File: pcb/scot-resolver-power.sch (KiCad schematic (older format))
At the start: 36 parts, among them IC4 TSR1, U1 MCP1703A-5002_SOT223, U2 LT1762, U3 MCP1703A-5002_SOT223, U4 MCP1703A-5002_SOT223, U5 MCP1703A-3302_SOT223

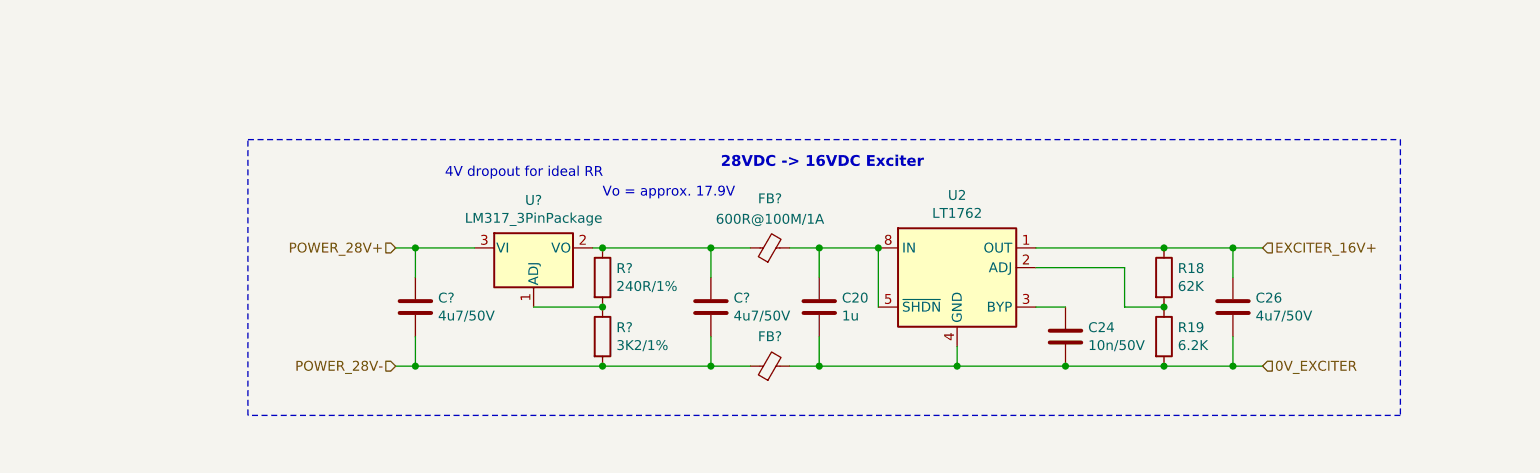
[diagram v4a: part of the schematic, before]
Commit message: pcb: V2 schematic updates (PCB still to do).
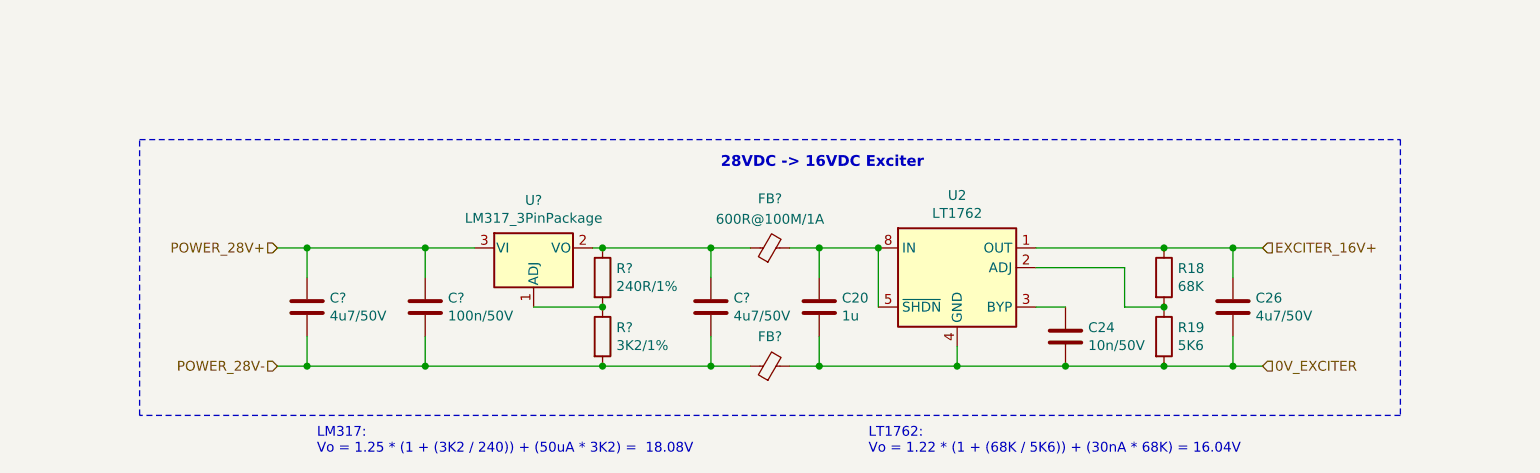
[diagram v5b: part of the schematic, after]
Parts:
- added C?: 100n/50V, Capacitor_SMD:C_0603_1608Metric_Pad1.05x0.95mm_HandSolder, symbol Device:C
- R18: value 62K -> 68K
- R19: value 6.2K -> 5K6
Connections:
- net POWER_28V+: now also C?.1
- net POWER_28V-: now also C?.2
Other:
- note added: "LM317:\nVo = 1.25 * (1 + (3K2 / 240)) + (50uA * 3K2) = 18.08V"
- note added: "LT1762:\nVo = 1.22 * (1 + (68K / 5K6)) + (30nA * 68K) = 16.04V"
- note removed: "4V dropout for ideal RR"
- note removed: "Vo = approx. 17.9V"
- moved on the sheet: C?
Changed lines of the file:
@@
 $Descr A4 11693 8268
 encoding utf-8
-Sheet 4 9
+Sheet 4 7
 Title ""
 Date ""
@@
 AR Path="/5E2C28ED/5E2DB019" Ref="R19"  Part="1"
 F 0 "R19" H 7020 5796 50  0000 L CNN
-F 1 "6.2K" H 7020 5705 50  0000 L CNN
+F 1 "5K6" H 7020 5705 50  0000 L CNN
 F 2 "Resistor_SMD:R_0603_1608Metric_Pad1.05x0.95mm_HandSolder" V 6880 5750 50  0001 C CNN
 F 3 "~" H 6950 5750 50  0001 C CNN
@@
 AR Path="/5E2C28ED/5E2DB01F" Ref="R18"  Part="1"
 F 0 "R18" H 7020 5496 50  0000 L CNN
-F 1 "62K" H 7020 5405 50  0000 L CNN
+F 1 "68K" H 7020 5405 50  0000 L CNN
 F 2 "Resistor_SMD:R_0603_1608Metric_Pad1.05x0.95mm_HandSolder" V 6880 5450 50  0001 C CNN
 F 3 "~" H 6950 5450 50  0001 C CNN
@@
 	8150 4750 8150 6150
 Wire Notes Line
-	2300 6150 2300 4750
+	1750 6150 1750 4750
 Text HLabel 2000 1700 0    50   Input ~ 0
 POWER_28V+
@@
 Connection ~ 2650 2000
 Wire Notes Line
-	2300 4750 8150 4750
-Wire Notes Line
-	8150 6150 2300 6150
+	1750 4750 8150 4750
+Wire Notes Line
+	8150 6150 1750 6150
 Wire Notes Line
 	7300 3950 10650 3950
@@
 L Device:C C?
 U 1 1 5E9EAF60
-P 3150 5600
+P 2600 5600
 AR Path="/5E9EAF60" Ref="C?"  Part="1"
 AR Path="/5E2C28ED/5E9EAF60" Ref="C?"  Part="1"
-F 0 "C?" H 3265 5646 50  0000 L CNN
-F 1 "4u7/50V" H 3265 5555 50  0000 L CNN
-F 2 "Capacitor_SMD:C_1206_3216Metric_Pad1.42x1.75mm_HandSolder" H 3188 5450 50  0001 C CNN
-F 3 "~" H 3150 5600 50  0001 C CNN
-	1    3150 5600
+F 0 "C?" H 2715 5646 50  0000 L CNN
+F 1 "4u7/50V" H 2715 5555 50  0000 L CNN
+F 2 "Capacitor_SMD:C_1206_3216Metric_Pad1.42x1.75mm_HandSolder" H 2638 5450 50  0001 C CNN
+F 3 "~" H 2600 5600 50  0001 C CNN
+	1    2600 5600
 	1    0    0    -1
 $EndComp
@@
 $EndComp
 Wire Wire Line
-	3150 5450 3150 5300
-Wire Wire Line
-	3150 5300 3450 5300
+	2600 5450 2600 5300
+Wire Wire Line
+	2600 5300 3200 5300
 Wire Wire Line
 	4050 5300 4100 5300
@@
 Connection ~ 4100 5300
 Wire Wire Line
-	4100 5900 3150 5900
-Wire Wire Line
-	3150 5900 3150 5750
+	4100 5900 3200 5900
+Wire Wire Line
+	2600 5900 2600 5750
 Connection ~ 4100 5900
-Text Notes 4100 5050 0    50   ~ 0
-Vo = approx. 17.9V
+Text Notes 2650 6350 0    50   ~ 0
+LM317:\nVo = 1.25 * (1 + (3K2 / 240)) + (50uA * 3K2) =  18.08V
 Text HLabel 7450 5900 2    50   Input ~ 0
 0V_EXCITER
@@
 	7450 5900 7300 5900
 Connection ~ 7300 5900
-Text Notes 3300 4950 0    50   ~ 0
-4V dropout for ideal RR
 Text Label 1050 3350 0    50   ~ 0
 DIGITAL_6.5V+
@@
 Wire Wire Line
 	5900 5900 6450 5900
-Text HLabel 3050 5300 0    50   Input ~ 0
+Text HLabel 2450 5300 0    50   Input ~ 0
 POWER_28V+
-Text HLabel 3050 5900 0    50   Input ~ 0
+Text HLabel 2450 5900 0    50   Input ~ 0
 POWER_28V-
 Wire Wire Line
-	3150 5900 3050 5900
-Connection ~ 3150 5900
-Wire Wire Line
-	3150 5300 3050 5300
-Connection ~ 3150 5300
+	2600 5900 2450 5900
+Connection ~ 2600 5900
+Wire Wire Line
+	2600 5300 2450 5300
+Connection ~ 2600 5300
 Text Label 4350 3650 0    50   ~ 0
 DIGITAL_6.5V-
@@
 Wire Wire Line
 	9200 3650 9550 3650
+$Comp
+L Device:C C?
+U 1 1 5EA792EE
+P 3200 5600
+AR Path="/5EA792EE" Ref="C?"  Part="1"
+AR Path="/5E2C28ED/5EA792EE" Ref="C?"  Part="1"
+F 0 "C?" H 3315 5646 50  0000 L CNN
+F 1 "100n/50V" H 3315 5555 50  0000 L CNN
+F 2 "Capacitor_SMD:C_0603_1608Metric_Pad1.05x0.95mm_HandSolder" H 3238 5450 50  0001 C CNN
+F 3 "~" H 3200 5600 50  0001 C CNN
+	1    3200 5600
+	1    0    0    -1
+$EndComp
+Wire Wire Line
+	3200 5750 3200 5900
+Connection ~ 3200 5900
+Wire Wire Line
+	3200 5900 2600 5900
+Wire Wire Line
+	3200 5450 3200 5300
+Connection ~ 3200 5300
+Wire Wire Line
+	3200 5300 3450 5300
+Text Notes 5450 6350 0    50   ~ 0
+LT1762:\nVo = 1.22 * (1 + (68K / 5K6)) + (30nA * 68K) = 16.04V
 $EndSCHEMATC

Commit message: pcb: Add 10u to VREF, all 0402->0603
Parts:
- U6: renamed from U?; footprint (none) -> Package_TO_SOT_SMD:SOT-223-3_TabPin2
- gave numbers to parts that had none: 7
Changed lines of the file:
@@
 Connection ~ 2150 1700
 $Comp
-L Regulator_Linear:LM317_3PinPackage U?
+L Regulator_Linear:LM317_3PinPackage U6
 U 1 1 5E9E6E0D
 P 3750 5300
-F 0 "U?" H 3750 5542 50  0000 C CNN
+F 0 "U6" H 3750 5542 50  0000 C CNN
 F 1 "LM317_3PinPackage" H 3750 5451 50  0000 C CNN
-F 2 "" H 3750 5550 50  0001 C CIN
+F 2 "Package_TO_SOT_SMD:SOT-223-3_TabPin2" H 3750 5550 50  0001 C CIN
 F 3 "http://www.ti.com/lit/ds/symlink/lm317.pdf" H 3750 5300 50  0001 C CNN
 	1    3750 5300
@@
 $EndComp
 $Comp
-L Device:R R?
+L Device:R R21
 U 1 1 5E9E84EF
 P 4100 5450
-F 0 "R?" H 4170 5496 50  0000 L CNN
+F 0 "R21" H 4170 5496 50  0000 L CNN
 F 1 "240R/1%" H 4170 5405 50  0000 L CNN
 F 2 "Resistor_SMD:R_0805_2012Metric_Pad1.15x1.40mm_HandSolder" V 4030 5450 50  0001 C CNN
@@
 $EndComp
 $Comp
-L Device:R R?
+L Device:R R22
 U 1 1 5E9E8F66
 P 4100 5750
-F 0 "R?" H 4170 5796 50  0000 L CNN
+F 0 "R22" H 4170 5796 50  0000 L CNN
 F 1 "3K2/1%" H 4170 5705 50  0000 L CNN
 F 2 "Resistor_SMD:R_0805_2012Metric_Pad1.15x1.40mm_HandSolder" V 4030 5750 50  0001 C CNN
@@
 P 2600 5600
 AR Path="/5E9EAF60" Ref="C?"  Part="1"
-AR Path="/5E2C28ED/5E9EAF60" Ref="C?"  Part="1"
-F 0 "C?" H 2715 5646 50  0000 L CNN
+AR Path="/5E2C28ED/5E9EAF60" Ref="C35"  Part="1"
+F 0 "C35" H 2715 5646 50  0000 L CNN
 F 1 "4u7/50V" H 2715 5555 50  0000 L CNN
 F 2 "Capacitor_SMD:C_1206_3216Metric_Pad1.42x1.75mm_HandSolder" H 2638 5450 50  0001 C CNN
@@
 P 4650 5600
 AR Path="/5E9F21C4" Ref="C?"  Part="1"
-AR Path="/5E2C28ED/5E9F21C4" Ref="C?"  Part="1"
-F 0 "C?" H 4765 5646 50  0000 L CNN
+AR Path="/5E2C28ED/5E9F21C4" Ref="C37"  Part="1"
+F 0 "C37" H 4765 5646 50  0000 L CNN
 F 1 "4u7/50V" H 4765 5555 50  0000 L CNN
 F 2 "Capacitor_SMD:C_0603_1608Metric_Pad1.05x0.95mm_HandSolder" H 4688 5450 50  0001 C CNN
@@
 	4400 2200 4950 2200
 $Comp
-L Device:Ferrite_Bead_Small FB?
+L Device:Ferrite_Bead_Small FB5
 U 1 1 5EAE90A0
 P 4950 5300
-F 0 "FB?" V 5200 5300 50  0000 C CNN
+F 0 "FB5" V 5200 5300 50  0000 C CNN
 F 1 "600R@100M/1A" V 5096 5300 50  0000 C CNN
 F 2 "Inductor_SMD:L_0805_2012Metric_Pad1.15x1.40mm_HandSolder" V 4880 5300 50  0001 C CNN
@@
 $EndComp
 $Comp
-L Device:Ferrite_Bead_Small FB?
+L Device:Ferrite_Bead_Small FB6
 U 1 1 5EAEAA70
 P 4950 5900
-F 0 "FB?" V 5100 5900 50  0000 C CNN
+F 0 "FB6" V 5100 5900 50  0000 C CNN
 F 1 "600R@100M/1A" V 5096 5900 50  0001 C CNN
 F 2 "Inductor_SMD:L_0805_2012Metric_Pad1.15x1.40mm_HandSolder" V 4880 5900 50  0001 C CNN
@@
 P 3200 5600
 AR Path="/5EA792EE" Ref="C?"  Part="1"
-AR Path="/5E2C28ED/5EA792EE" Ref="C?"  Part="1"
-F 0 "C?" H 3315 5646 50  0000 L CNN
+AR Path="/5E2C28ED/5EA792EE" Ref="C36"  Part="1"
+F 0 "C36" H 3315 5646 50  0000 L CNN
 F 1 "100n/50V" H 3315 5555 50  0000 L CNN
 F 2 "Capacitor_SMD:C_0603_1608Metric_Pad1.05x0.95mm_HandSolder" H 3238 5450 50  0001 C CNN

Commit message: pcb: Add v2 BOM, fix some component values.
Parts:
- C20: value 1u -> 1u/50V
- C37: value 4u7/50V -> 1u/50V
- R22: value 3K2/1% -> 3K3/1%
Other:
- note added: "LM317:\nVo = 1.25 * (1 + (3K3 / 240)) + (50uA * 3K3) = 18.60V"
- note removed: "LM317:\nVo = 1.25 * (1 + (3K2 / 240)) + (50uA * 3K2) = 18.08V"
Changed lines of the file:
@@
 $Descr A4 11693 8268
 encoding utf-8
-Sheet 4 7
+Sheet 3 7
 Title ""
 Date ""
@@
 AR Path="/5E2C28ED/5E3070F3" Ref="C20"  Part="1"
 F 0 "C20" H 5315 5646 50  0000 L CNN
-F 1 "1u" H 5315 5555 50  0000 L CNN
+F 1 "1u/50V" H 5315 5555 50  0000 L CNN
 F 2 "Capacitor_SMD:C_0603_1608Metric_Pad1.05x0.95mm_HandSolder" H 5238 5450 50  0001 C CNN
 F 3 "~" H 5200 5600 50  0001 C CNN
@@
 P 4100 5750
 F 0 "R22" H 4170 5796 50  0000 L CNN
-F 1 "3K2/1%" H 4170 5705 50  0000 L CNN
+F 1 "3K3/1%" H 4170 5705 50  0000 L CNN
 F 2 "Resistor_SMD:R_0805_2012Metric_Pad1.15x1.40mm_HandSolder" V 4030 5750 50  0001 C CNN
 F 3 "~" H 4100 5750 50  0001 C CNN
@@
 AR Path="/5E2C28ED/5E9F21C4" Ref="C37"  Part="1"
 F 0 "C37" H 4765 5646 50  0000 L CNN
-F 1 "4u7/50V" H 4765 5555 50  0000 L CNN
+F 1 "1u/50V" H 4765 5555 50  0000 L CNN
 F 2 "Capacitor_SMD:C_0603_1608Metric_Pad1.05x0.95mm_HandSolder" H 4688 5450 50  0001 C CNN
 F 3 "~" H 4650 5600 50  0001 C CNN
@@
 Connection ~ 4100 5900
 Text Notes 2650 6350 0    50   ~ 0
-LM317:\nVo = 1.25 * (1 + (3K2 / 240)) + (50uA * 3K2) =  18.08V
+LM317:\nVo = 1.25 * (1 + (3K3 / 240)) + (50uA * 3K3) =  18.60V
 Text HLabel 7450 5900 2    50   Input ~ 0
 0V_EXCITER
